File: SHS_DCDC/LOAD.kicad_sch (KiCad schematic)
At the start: 36 parts, among them Q2 PMV100XPEAR, Q3 2N7002, Q4 2N7002, Q5 PMV100XPEAR, Q6 2N7002, Q7 PMV100XPEAR

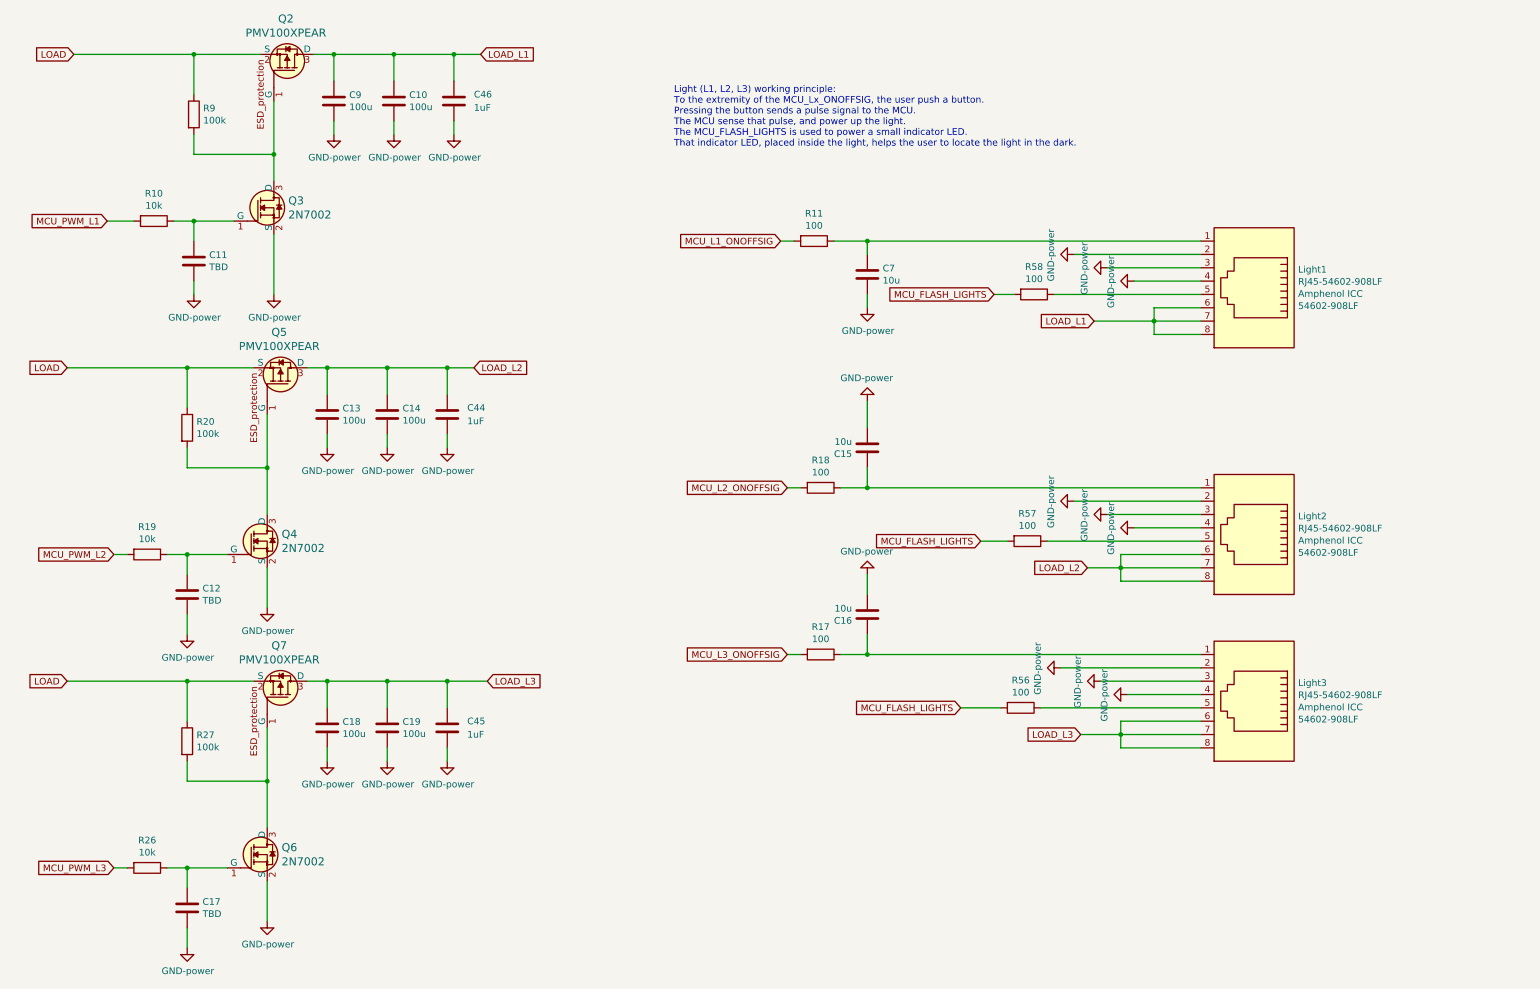
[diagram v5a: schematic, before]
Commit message: Commit before reannotation
Plan to test the reannotation feature.
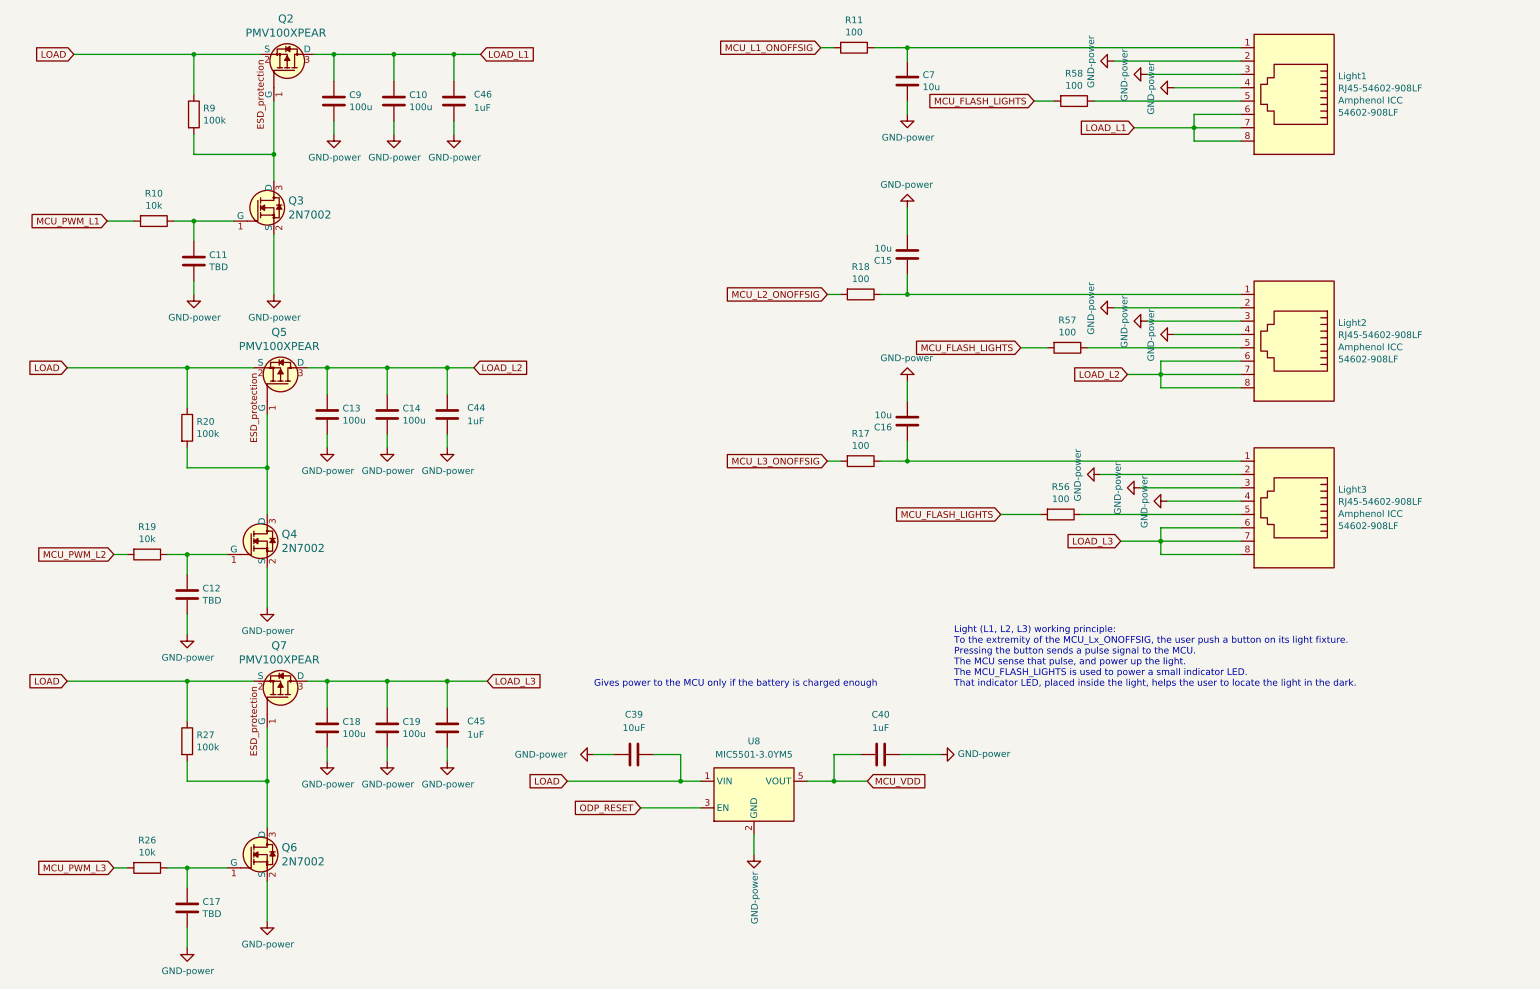
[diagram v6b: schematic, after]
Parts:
- added C39: 10uF, Capacitor_SMD:C_0805_2012Metric, symbol Device:C
- added C40: 1uF, Capacitor_SMD:C_0603_1608Metric, symbol Device:C
- added U8: MIC5501-3.0YM5, Package_TO_SOT_SMD:SOT-23-5, symbol Regulator_Linear:MIC5501-3.0YM5
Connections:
- net GND: now also C39.1, C40.2, U8.2 (GND)
- net LOAD: now also C39.2, U8.1 (VIN)
- new net MCU_VDD: C40.1, U8.5 (VOUT)
- new net ODP_RESET: U8.3 (EN)
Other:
- note added: "Gives power to the MCU only if the battery is charged enough"
- note added: "Light (L1, L2, L3) working principle: To the extremity of the MCU_Lx_ONOFFSIG, the user push a button on its light fixture. Pressing the button sends a pulse signal to the MCU. The MCU sense that pulse, and power up the light. The MCU_FLASH_LIGHTS is used to power a small indicator LED. That indicator LED, placed inside the light, helps the user to locate the light in the dark."
- note removed: "Light (L1, L2, L3) working principle: To the extremity of the MCU_Lx_ONOFFSIG, the user push a button. Pressing the button sends a pulse signal to the MCU. The MCU sense that pulse, and power up the light. The MCU_FLASH_LIGHTS is used to power a small indicator LED. That indicator LED, placed inside the light, helps the user to locate the light in the dark."
- moved on the sheet: C15, C16, C7, Light1, Light2, Light3, R11, R17, R18, R56, R57, R58

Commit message: Testpoints
All the tests points have been placed
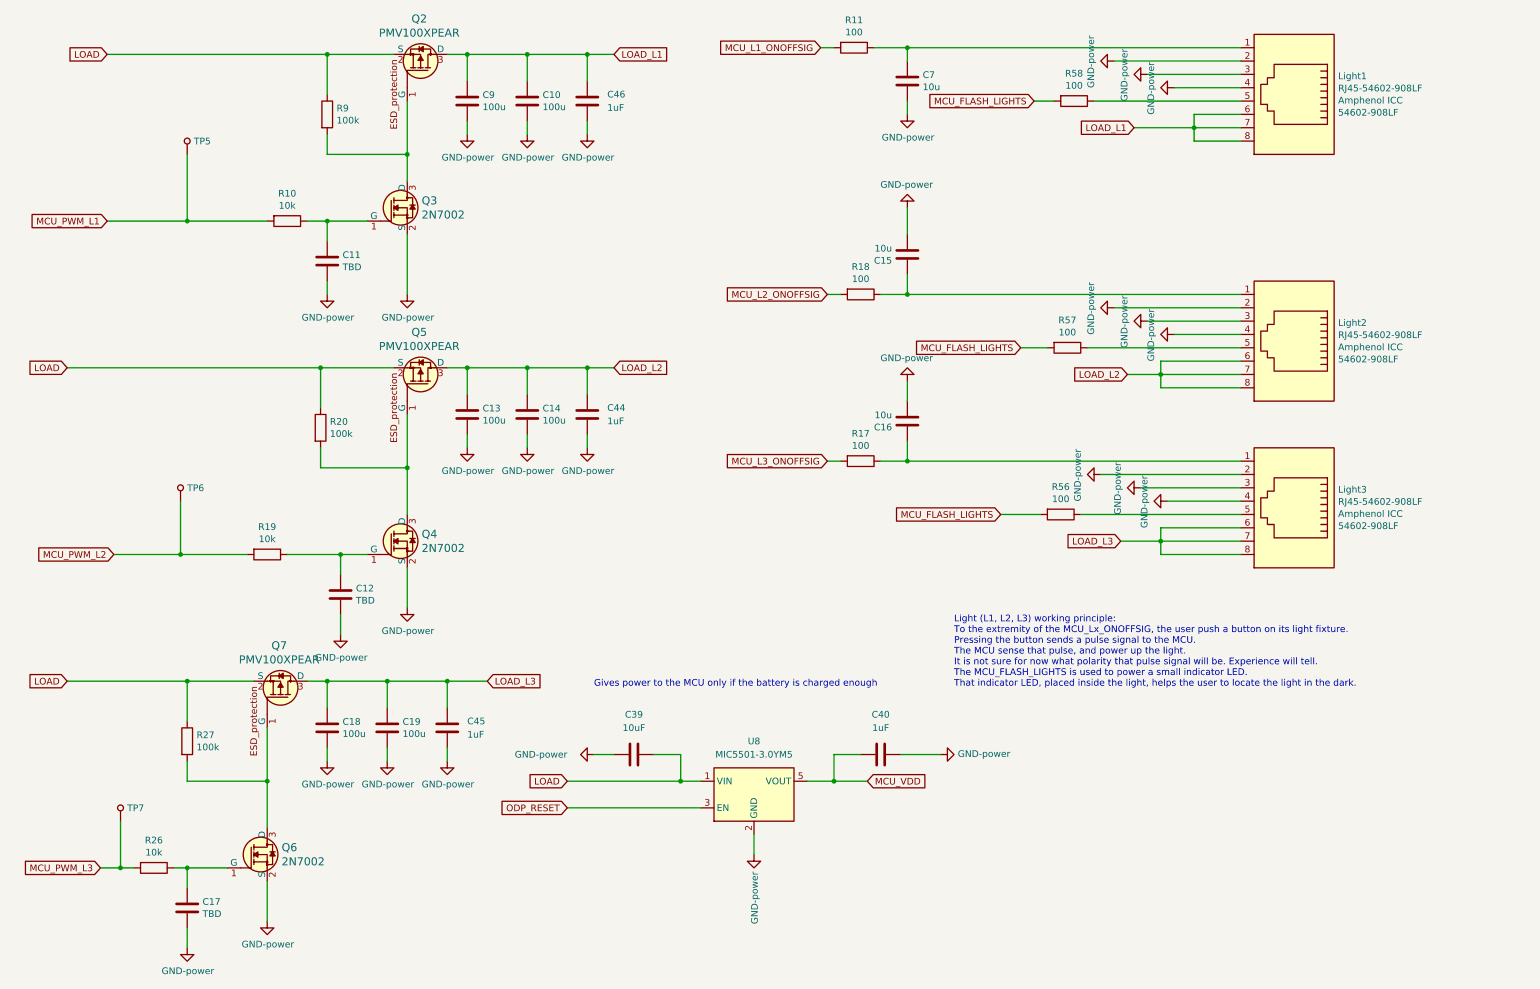
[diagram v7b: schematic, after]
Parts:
- added TP5, TP6, TP7: 5029, digikey-footprints:PC_Test_Point_Mini_3.8x2.03mm, symbol dk_Test-Points:5029
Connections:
- net MCU_PWM_L1: now also TP5.1
- net MCU_PWM_L2: now also TP6.1
- net MCU_PWM_L3: now also TP7.1
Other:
- note added: "Light (L1, L2, L3) working principle: To the extremity of the MCU_Lx_ONOFFSIG, the user push a button on its light fixture. Pressing the button sends a pulse signal to the MCU. The MCU sense that pulse, and power up the light. It is not sure for now what polarity that pulse signal will be. Experience will tell. The MCU_FLASH_LIGHTS is used to power a small indicator LED. That indicator LED, place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"
- note removed: "Light (L1, L2, L3) working principle: To the extremity of the MCU_Lx_ONOFFSIG, the user push a button on its light fixture. Pressing the button sends a pulse signal to the MCU. The MCU sense that pulse, and power up the light. The MCU_FLASH_LIGHTS is used to power a small indicator LED. That indicator LED, placed inside the light, helps the user to locate the light in the dark."
- moved on the sheet: C10, C11, C12, C13, C14, C44, C46, C9, Q2, Q3, Q4, Q5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

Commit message: Gerber
Gerber output, ready to send to JLCPCB
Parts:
- added TP19: 5029, digikey-footprints:PC_Test_Point_Mini_3.8x2.03mm, symbol dk_Test-Points:5029
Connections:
- net MCU_VDD: now also TP19.1
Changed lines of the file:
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@@
     (stroke (width 0) (type default) (color 0 0 0 0))
   )
-  (wire (pts (xy 167.64 160.02) (xy 173.99 160.02))
+  (wire (pts (xy 167.64 160.02) (xy 180.34 160.02))
     (stroke (width 0) (type default) (color 0 0 0 0))
   )
@@
   )
   (wire (pts (xy 44.45 53.34) (xy 29.21 53.34))
+    (stroke (width 0) (type default) (color 0 0 0 0))
+  )
+  (wire (pts (xy 167.64 160.02) (xy 167.64 167.64))
     (stroke (width 0) (type default) (color 0 0 0 0))
   )
@@
     )
   )
-  (global_label "MCU_VDD" (shape input) (at 173.99 160.02 0) (fields_autoplaced)
+  (global_label "MCU_VDD" (shape input) (at 180.34 160.02 0) (fields_autoplaced)
     (effects (font (size 1.27 1.27)) (justify left))
-    (property "Intersheet References" "${INTERSHEET_REFS}" (id 0) (at 184.9623 159.9406 0)
+    (property "Intersheet References" "${INTERSHEET_REFS}" (id 0) (at 191.3123 159.9406 0)
       (effects (font (size 1.27 1.27)) (justify left) hide)
     )
@@
     )
     (pin "1")
+  )
+  (symbol (lib_id "dk_Test-Points:5029") (at 167.64 170.18 0) (unit 1)
+    (in_bom yes) (on_board yes) (fields_autoplaced)
+    (property "Reference" "TP19" (id 0) (at 168.91 170.1418 0)
+      (effects (font (size 1.27 1.27)) (justify left))
+    )
+    (property "Value" "5029" (id 1) (at 167.64 172.72 0)
+      (effects (font (size 1.27 1.27)) hide)
+    )
+    (property "Footprint" "digikey-footprints:PC_Test_Point_Mini_3.8x2.03mm" (id 2) (at 172.72 165.1 0)
+      (effects (font (size 1.524 1.524)) (justify left) hide)
+    )
+    (property "Datasheet" "http://www.keyelco.com/product-pdf.cfm?p=1358" (id 3) (at 172.72 162.56 0)
+      (effects (font (size 1.524 1.524)) (justify left) hide)
+    )
+    (property "Digi-Key_PN" "36-5029CT-ND" (id 4) (at 172.72 160.02 0)
+      (effects (font (size 1.524 1.524)) (justify left) hide)
+    )
+    (property "MPN" "5029" (id 5) (at 172.72 157.48 0)
+      (effects (font (size 1.524 1.524)) (justify left) hide)
+    )
+    (property "Category" "Test and Measurement" (id 6) (at 172.72 154.94 0)
+      (effects (font (size 1.524 1.524)) (justify left) hide)
+    )
+    (property "Family" "Test Points" (id 7) (at 172.72 152.4 0)
+      (effects (font (size 1.524 1.524)) (justify left) hide)
+    )
+    (property "DK_Datasheet_Link" "http://www.keyelco.com/product-pdf.cfm?p=1358" (id 8) (at 172.72 149.86 0)
+      (effects (font (size 1.524 1.524)) (justify left) hide)
+    )
+    (property "DK_Detail_Page" "/product-detail/en/keystone-electronics/5029/36-5029CT-ND/5980631" (id 9) (at 172.72 147.32 0)
+      (effects (font (size 1.524 1.524)) (justify left) hide)
+    )
+    (property "Description" "PC TEST POINT MINIATURE" (id 10) (at 172.72 144.78 0)
+      (effects (font (size 1.524 1.524)) (justify left) hide)
+    )
+    (property "Manufacturer" "Keystone Electronics" (id 11) (at 172.72 142.24 0)
+      (effects (font (size 1.524 1.524)) (justify left) hide)
+    )
+    (property "Status" "Active" (id 12) (at 172.72 139.7 0)
+      (effects (font (size 1.524 1.524)) (justify left) hide)
+    )
+    (pin "1")
